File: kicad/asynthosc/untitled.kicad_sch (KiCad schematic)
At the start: 6 parts, among them J13 AudioJack3, U12 H11L1

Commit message: bom: add jlcpcb field with simplified footprint
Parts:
- D15: JLC (none) -> SOD-523
- R68, R69: JLC (none) -> 0402
- U12: JLC (none) -> SMDIP-6
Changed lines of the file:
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@@
+			)
+		)
+		(property "JLC" "SMDIP-6"
+			(at 240.03 50.8 0)
+			(effects
+				(font
+					(size 1.27 1.27)
+				)
+				(hide yes)
 			)
 		)
@@
 			)
 		)
+		(property "JLC" "SOD-523"
+			(at 219.71 52.07 0)
+			(effects
+				(font
+					(size 1.27 1.27)
+				)
+				(hide yes)
+			)
+		)
 		(pin "2"
 		)
@@
 			)
 		)
+		(property "JLC" ""
+			(at 185.42 50.8 0)
+			(effects
+				(font
+					(size 1.27 1.27)
+				)
+				(hide yes)
+			)
+		)
 		(pin "S"
 		)
@@
 			)
 		)
+		(property "JLC" "0402"
+			(at 212.09 48.26 0)
+			(effects
+				(font
+					(size 1.27 1.27)
+				)
+				(hide yes)
+			)
+		)
 		(pin "1"
 		)
@@
 			)
 		)
+		(property "JLC" ""
+			(at 201.93 48.26 0)
+			(effects
+				(font
+					(size 1.27 1.27)
+				)
+				(hide yes)
+			)
+		)
 		(pin "1"
 		)
@@
 			(at 255.27 44.45 0)
 			(effects
+				(font
+					(size 1.27 1.27)
+				)
+				(hide yes)
+			)
+		)
+		(property "JLC" "0402"
+			(at 255.27 44.45 0)
+			(effects

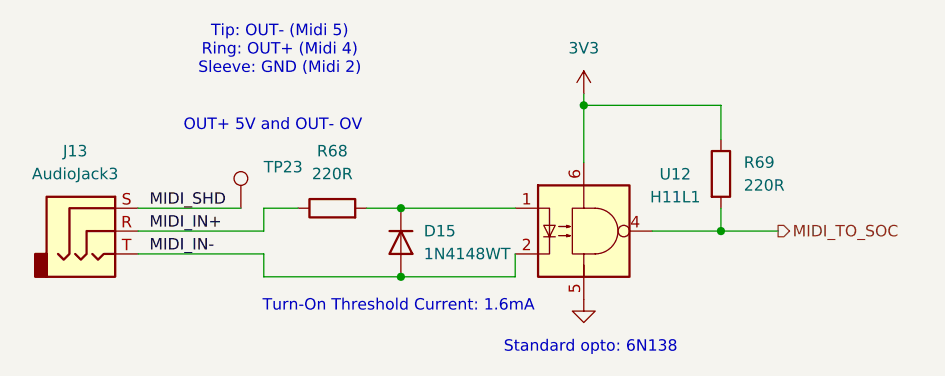
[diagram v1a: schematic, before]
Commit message: bom: dnp for all manually equiped components
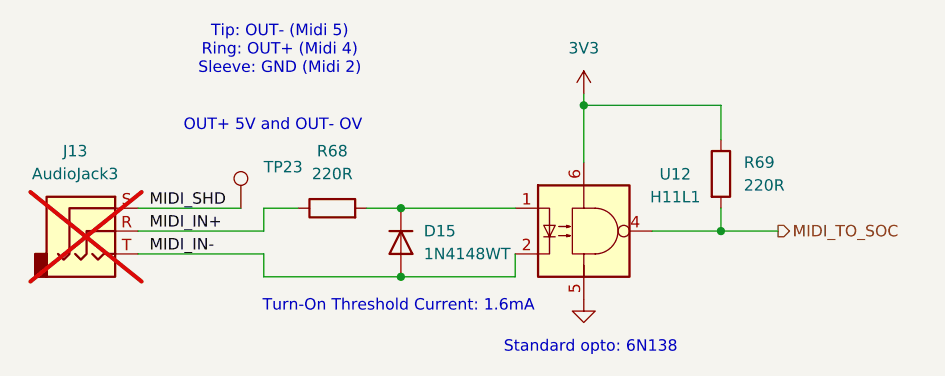
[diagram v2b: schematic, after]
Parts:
- J13: now not fitted
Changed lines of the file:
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@@
 		(in_bom yes)
 		(on_board yes)
-		(dnp no)
+		(dnp yes)
 		(fields_autoplaced yes)
 		(property "Reference" "J13"

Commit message: bom: adding jlc ref to generic
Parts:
- R68, R69: LCSC (none) -> C279989
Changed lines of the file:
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@@
 			)
 		)
-		(property "LCSC" ""
+		(property "LCSC" " C279989"
 			(at 212.09 48.26 0)
 			(effects
@@
 			)
 		)
-		(property "LCSC" ""
+		(property "LCSC" " C279989"
 			(at 255.27 44.45 0)
 			(effects
